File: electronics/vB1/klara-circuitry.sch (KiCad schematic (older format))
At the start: 15 parts, among them J1 Pin header, U1 MCP1700-3302E, U3 ATtiny85

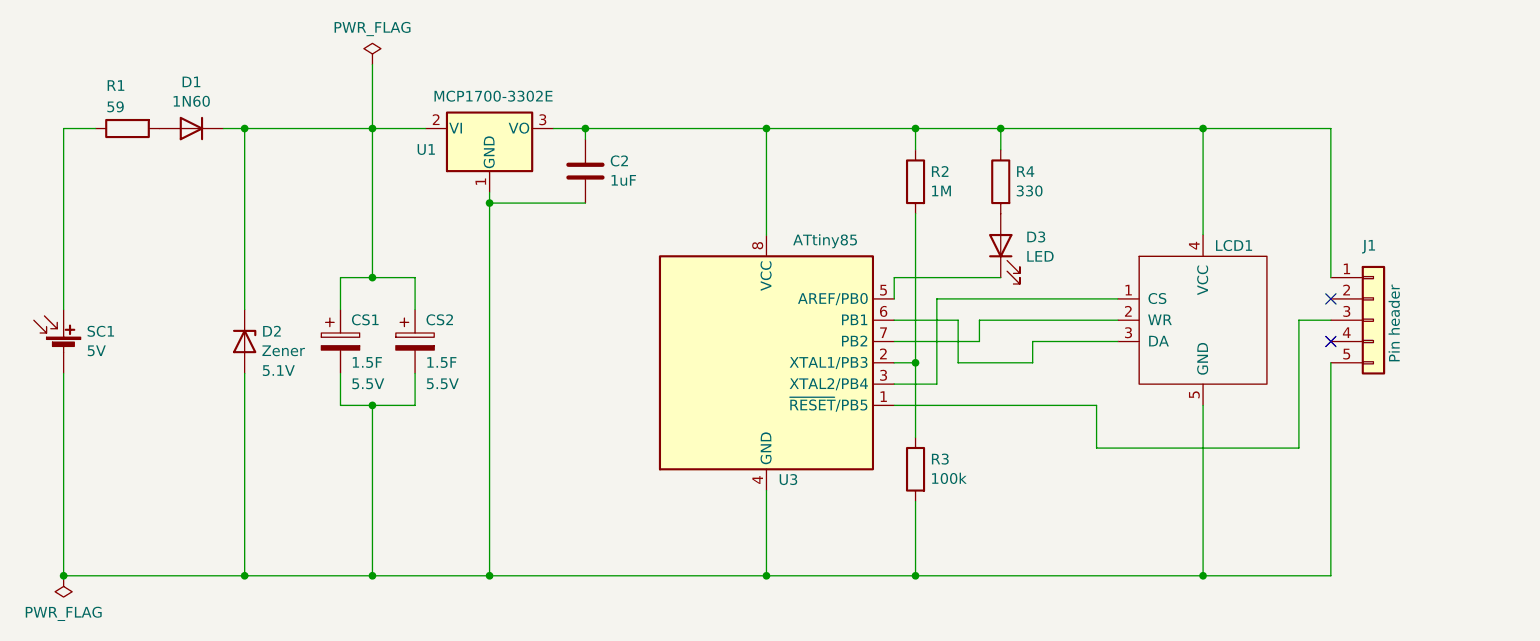
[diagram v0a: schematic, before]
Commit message: circuit d'oh: measure supercap voltage, not regulator output
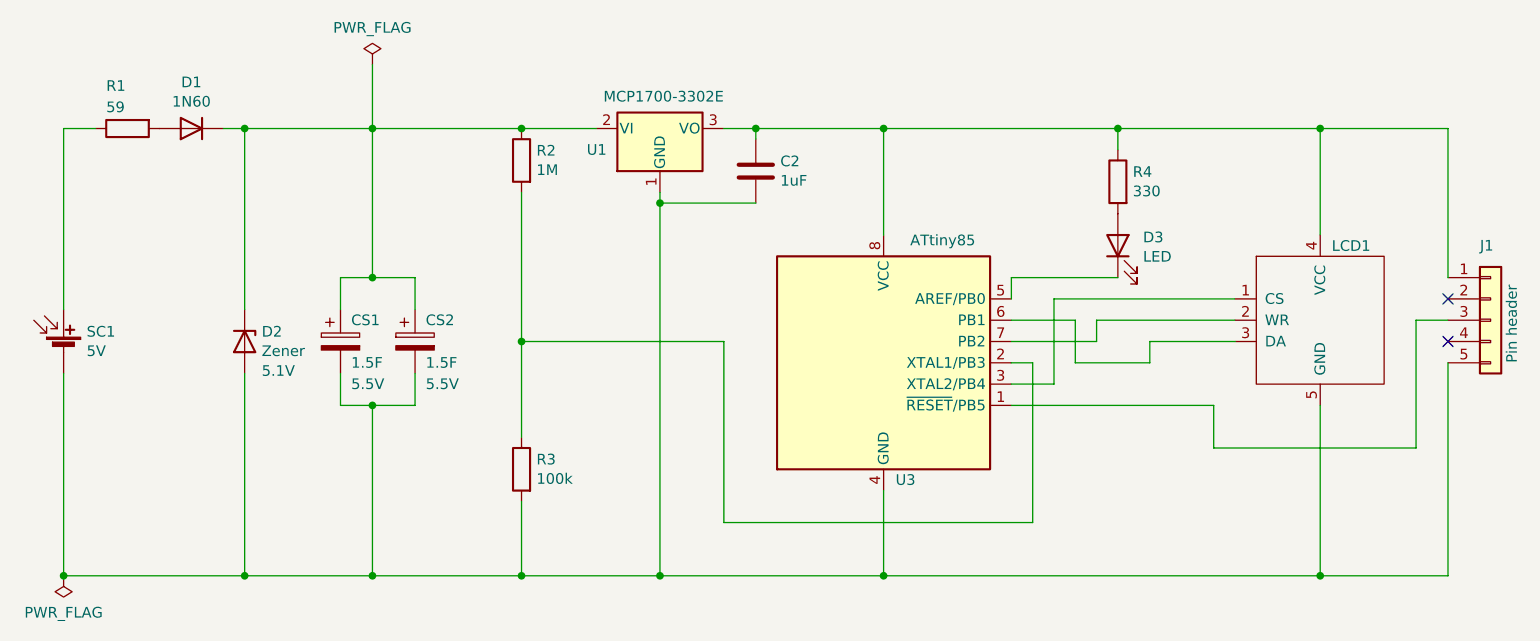
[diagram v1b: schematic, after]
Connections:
- net at C2.1, J1.1 (Pin_1), LCD1.4 (VCC)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: no longer R2.1
- net at CS1.1, CS2.1, D1.1 (K)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: now also R2.1
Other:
- moved on the sheet: C2, D3, J1, LCD1, R2, R3, R4, U1, U3
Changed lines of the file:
@@
 	1500 2600 1500 1750
 Wire Wire Line
-	4800 3450 4800 3850
+	5350 3450 5350 3850
 $Comp
 L Device:D_Zener D2
@@
 $EndComp
 Wire Wire Line
-	4800 1750 4800 2250
-Wire Wire Line
-	5600 2950 5600 2550
+	5350 1750 5350 2250
+Wire Wire Line
+	6150 2950 6150 2550
 $Comp
 L Display_Character:HT1621 LCD1
 U 1 1 62A78604
-P 6850 2750
-F 0 "LCD1" H 6904 3228 50  0000 L TNN
-F 1 "HT1621" H 7178 2805 50  0001 L CNN
-F 2 "Display_7Segment:LCD_SPI" H 7050 3200 50  0001 C CNN
-F 3 "" H 7050 3200 50  0001 C CNN
-	1    6850 2750
-	1    0    0    -1
-$EndComp
-Wire Wire Line
-	5400 2650 5700 2650
-Wire Wire Line
-	5400 2950 5600 2950
+P 7400 2750
+F 0 "LCD1" H 7454 3228 50  0000 L TNN
+F 1 "HT1621" H 7728 2805 50  0001 L CNN
+F 2 "Display_7Segment:LCD_SPI" H 7600 3200 50  0001 C CNN
+F 3 "" H 7600 3200 50  0001 C CNN
+	1    7400 2750
+	1    0    0    -1
+$EndComp
+Wire Wire Line
+	5950 2650 6250 2650
+Wire Wire Line
+	5950 2950 6150 2950
 Wire Wire Line
 	1500 3850 1500 2900
@@
 L Regulator_Linear:MCP1700-3302E_TO92 U1
 U 1 1 62AF9A6C
-P 3500 1750
-F 0 "U1" H 3250 1850 50  0000 R CNN
-F 1 "MCP1700-3302E" H 3800 1600 50  0000 R CNN
-F 2 "Package_TO_SOT_THT:TO-92_Inline_Wide" H 3500 1550 50  0001 C CIN
-F 3 "http://ww1.microchip.com/downloads/en/DeviceDoc/20001826D.pdf" H 3500 1750 50  0001 C CNN
-	1    3500 1750
+P 4300 1750
+F 0 "U1" H 4050 1850 50  0000 R CNN
+F 1 "MCP1700-3302E" H 4600 1600 50  0000 R CNN
+F 2 "Package_TO_SOT_THT:TO-92_Inline_Wide" H 4300 1550 50  0001 C CIN
+F 3 "http://ww1.microchip.com/downloads/en/DeviceDoc/20001826D.pdf" H 4300 1750 50  0001 C CNN
+	1    4300 1750
 	1    0    0    1
 $EndComp
 Wire Wire Line
-	5700 2850 5700 2650
-Wire Wire Line
-	3500 2050 3500 2100
-Wire Wire Line
-	5800 2650 5800 2750
-Wire Wire Line
-	5800 2750 5400 2750
+	6250 2850 6250 2650
+Wire Wire Line
+	4300 2050 4300 2100
+Wire Wire Line
+	6350 2650 6350 2750
+Wire Wire Line
+	6350 2750 5950 2750
 $Comp
 L Device:R R4
 U 1 1 62B13E26
-P 5900 2000
-F 0 "R4" H 5830 2046 50  0000 R CNN
-F 1 "330" H 5830 1955 50  0000 R CNN
-F 2 "Resistor_THT:R_Axial_DIN0207_L6.3mm_D2.5mm_P10.16mm_Horizontal" V 5830 2000 50  0001 C CNN
-F 3 "~" H 5900 2000 50  0001 C CNN
-	1    5900 2000
+P 6450 2000
+F 0 "R4" H 6380 2046 50  0000 R CNN
+F 1 "330" H 6380 1955 50  0000 R CNN
+F 2 "Resistor_THT:R_Axial_DIN0207_L6.3mm_D2.5mm_P10.16mm_Horizontal" V 6380 2000 50  0001 C CNN
+F 3 "~" H 6450 2000 50  0001 C CNN
+	1    6450 2000
 	-1   0    0    -1
 $EndComp
@@
 L Device:LED D3
 U 1 1 62B14898
-P 5900 2300
-F 0 "D3" V 5939 2182 50  0000 R CNN
-F 1 "LED" V 5848 2182 50  0000 R CNN
-F 2 "LED_THT:LED_D5.0mm" H 5900 2300 50  0001 C CNN
-F 3 "~" H 5900 2300 50  0001 C CNN
-	1    5900 2300
+P 6450 2300
+F 0 "D3" V 6489 2182 50  0000 R CNN
+F 1 "LED" V 6398 2182 50  0000 R CNN
+F 2 "LED_THT:LED_D5.0mm" H 6450 2300 50  0001 C CNN
+F 3 "~" H 6450 2300 50  0001 C CNN
+	1    6450 2300
 	0    -1   -1   0
 $EndComp
 Wire Wire Line
-	4800 1750 5500 1750
-Wire Wire Line
-	3800 1750 3950 1750
+	4600 1750 4750 1750
 $Comp
 L Device:C C2
 U 1 1 62B08E4B
-P 3950 1950
-F 0 "C2" H 4065 1996 50  0000 L CNN
-F 1 "1uF" H 4065 1905 50  0000 L CNN
-F 2 "Capacitor_THT:C_Rect_L7.0mm_W2.0mm_P5.00mm" H 3988 1800 50  0001 C CNN
-F 3 "~" H 3950 1950 50  0001 C CNN
-	1    3950 1950
-	1    0    0    -1
-$EndComp
-Wire Wire Line
-	3950 1800 3950 1750
-Wire Wire Line
-	3950 2100 3500 2100
-Connection ~ 3500 2100
-Wire Wire Line
-	3500 2100 3500 3850
+P 4750 1950
+F 0 "C2" H 4865 1996 50  0000 L CNN
+F 1 "1uF" H 4865 1905 50  0000 L CNN
+F 2 "Capacitor_THT:C_Rect_L7.0mm_W2.0mm_P5.00mm" H 4788 1800 50  0001 C CNN
+F 3 "~" H 4750 1950 50  0001 C CNN
+	1    4750 1950
+	1    0    0    -1
+$EndComp
+Wire Wire Line
+	4750 1800 4750 1750
+Wire Wire Line
+	4750 2100 4300 2100
+Connection ~ 4300 2100
+Wire Wire Line
+	4300 2100 4300 3850
 $Comp
 L Device:R R2
 U 1 1 62B0AC42
-P 5500 2000
-F 0 "R2" H 5430 2046 50  0000 R CNN
-F 1 "1M" H 5430 1955 50  0000 R CNN
-F 2 "Resistor_THT:R_Axial_DIN0207_L6.3mm_D2.5mm_P10.16mm_Horizontal" V 5430 2000 50  0001 C CNN
-F 3 "~" H 5500 2000 50  0001 C CNN
-	1    5500 2000
+P 3650 1900
+F 0 "R2" H 3580 1946 50  0000 R CNN
+F 1 "1M" H 3580 1855 50  0000 R CNN
+F 2 "Resistor_THT:R_Axial_DIN0207_L6.3mm_D2.5mm_P10.16mm_Horizontal" V 3580 1900 50  0001 C CNN
+F 3 "~" H 3650 1900 50  0001 C CNN
+	1    3650 1900
 	-1   0    0    -1
 $EndComp
@@
 L Device:R R3
 U 1 1 62B0C047
-P 5500 3350
-F 0 "R3" H 5430 3396 50  0000 R CNN
-F 1 "100k" H 5430 3305 50  0000 R CNN
-F 2 "Resistor_THT:R_Axial_DIN0207_L6.3mm_D2.5mm_P10.16mm_Horizontal" V 5430 3350 50  0001 C CNN
-F 3 "~" H 5500 3350 50  0001 C CNN
-	1    5500 3350
+P 3650 3350
+F 0 "R3" H 3580 3396 50  0000 R CNN
+F 1 "100k" H 3580 3305 50  0000 R CNN
+F 2 "Resistor_THT:R_Axial_DIN0207_L6.3mm_D2.5mm_P10.16mm_Horizontal" V 3580 3350 50  0001 C CNN
+F 3 "~" H 3650 3350 50  0001 C CNN
+	1    3650 3350
 	-1   0    0    -1
 $EndComp
 Wire Wire Line
-	5500 1850 5500 1750
-Connection ~ 5500 1750
-Wire Wire Line
-	5400 2850 5500 2850
-Wire Wire Line
-	5500 2850 5500 2150
+	5950 2850 6050 2850
 Connection ~ 2350 3850
 Wire Wire Line
@@
 Connection ~ 2350 1750
 Wire Wire Line
-	5500 1750 5900 1750
-Wire Wire Line
-	5900 1850 5900 1750
-Wire Wire Line
-	5900 2450 5400 2450
-Wire Wire Line
-	5400 2450 5400 2550
-Wire Wire Line
-	5700 2850 6050 2850
-Wire Wire Line
-	6050 2850 6050 2750
-Wire Wire Line
-	5600 2550 6450 2550
-Wire Wire Line
-	5800 2650 6450 2650
-Wire Wire Line
-	6050 2750 6450 2750
-Wire Wire Line
-	5400 3050 6350 3050
-Wire Wire Line
-	6850 3850 6850 3050
-Connection ~ 5900 1750
-Wire Wire Line
-	6850 1750 6850 2250
+	6450 1850 6450 1750
+Wire Wire Line
+	6450 2450 5950 2450
+Wire Wire Line
+	5950 2450 5950 2550
+Wire Wire Line
+	6250 2850 6600 2850
+Wire Wire Line
+	6600 2850 6600 2750
+Wire Wire Line
+	6150 2550 7000 2550
+Wire Wire Line
+	6350 2650 7000 2650
+Wire Wire Line
+	6600 2750 7000 2750
+Wire Wire Line
+	5950 3050 6900 3050
+Wire Wire Line
+	7400 3850 7400 3050
+Connection ~ 6450 1750
+Wire Wire Line
+	7400 1750 7400 2250
 Wire Wire Line
 	2350 3850 2950 3850
@@
 Connection ~ 2950 3850
 Wire Wire Line
-	2950 3850 3500 3850
-Wire Wire Line
 	2950 2450 2950 1750
 Wire Wire Line
@@
 Connection ~ 2950 1750
 Wire Wire Line
-	2950 1750 3200 1750
-Wire Wire Line
-	6850 3850 7450 3850
-Connection ~ 6850 3850
-Wire Wire Line
-	7300 2650 7300 3250
-Wire Wire Line
-	7300 3250 6350 3250
-Wire Wire Line
-	6350 3250 6350 3050
-Wire Wire Line
-	7300 2650 7450 2650
-Wire Wire Line
-	6850 1750 7450 1750
-Connection ~ 6850 1750
-Wire Wire Line
-	4800 3850 5500 3850
-Wire Wire Line
-	5500 2850 5500 3200
-Connection ~ 5500 2850
-Wire Wire Line
-	5500 3500 5500 3850
-Connection ~ 5500 3850
-Wire Wire Line
-	5500 3850 6850 3850
+	7400 3850 8000 3850
+Connection ~ 7400 3850
+Wire Wire Line
+	7850 2650 7850 3250
+Wire Wire Line
+	7850 3250 6900 3250
+Wire Wire Line
+	6900 3250 6900 3050
+Wire Wire Line
+	7850 2650 8000 2650
+Wire Wire Line
+	7400 1750 8000 1750
+Connection ~ 7400 1750
+Wire Wire Line
+	3650 3500 3650 3850
 $Comp
 L MCU_Microchip_ATtiny:ATtiny85-20PU U3
 U 1 1 62A64AD0
-P 4800 2850
-F 0 "U3" H 4950 2300 50  0000 R CNN
-F 1 "ATtiny85" H 5231 3425 50  0000 R CNN
-F 2 "Package_DIP:DIP-8_W7.62mm" H 4800 2850 50  0001 C CIN
-F 3 "http://ww1.microchip.com/downloads/en/DeviceDoc/atmel-2586-avr-8-bit-microcontroller-attiny25-attiny45-attiny85_datasheet.pdf" H 4800 2850 50  0001 C CNN
-	1    4800 2850
+P 5350 2850
+F 0 "U3" H 5500 2300 50  0000 R CNN
+F 1 "ATtiny85" H 5781 3425 50  0000 R CNN
+F 2 "Package_DIP:DIP-8_W7.62mm" H 5350 2850 50  0001 C CIN
+F 3 "http://ww1.microchip.com/downloads/en/DeviceDoc/atmel-2586-avr-8-bit-microcontroller-attiny25-attiny45-attiny85_datasheet.pdf" H 5350 2850 50  0001 C CNN
+	1    5350 2850
 	1    0    0    -1
 $EndComp
@@
 	2950 1450 2950 1750
 Wire Wire Line
-	5900 1750 6850 1750
-Wire Wire Line
-	3950 1750 4800 1750
-Connection ~ 3950 1750
-Connection ~ 4800 1750
-Wire Wire Line
-	3500 3850 4800 3850
-Connection ~ 3500 3850
-Connection ~ 4800 3850
+	6450 1750 7400 1750
 $Comp
 L Connector_Generic:Conn_01x05 J1
 U 1 1 62D16CCC
-P 7650 2650
-F 0 "J1" H 7600 3000 50  0000 L CNN
-F 1 "Pin header" V 7750 2450 50  0000 L CNN
-F 2 "Connector_PinHeader_2.54mm:PinHeader_1x05_P2.54mm_Vertical" H 7650 2650 50  0001 C CNN
-F 3 "~" H 7650 2650 50  0001 C CNN
-	1    7650 2650
-	1    0    0    -1
-$EndComp
-Wire Wire Line
-	7450 2850 7450 3850
-Wire Wire Line
-	7450 1750 7450 2450
-NoConn ~ 7450 2550
-NoConn ~ 7450 2750
+P 8200 2650
+F 0 "J1" H 8150 3000 50  0000 L CNN
+F 1 "Pin header" V 8300 2450 50  0000 L CNN
+F 2 "Connector_PinHeader_2.54mm:PinHeader_1x05_P2.54mm_Vertical" H 8200 2650 50  0001 C CNN
+F 3 "~" H 8200 2650 50  0001 C CNN
+	1    8200 2650
+	1    0    0    -1
+$EndComp
+Wire Wire Line
+	8000 2850 8000 3850
+Wire Wire Line
+	8000 1750 8000 2450
+NoConn ~ 8000 2550
+NoConn ~ 8000 2750
+Wire Wire Line
+	5350 3850 7400 3850
+Wire Wire Line
+	2950 3850 3650 3850
+Connection ~ 5350 3850
+Connection ~ 3650 3850
+Wire Wire Line
+	3650 3850 4300 3850
+Connection ~ 4300 3850
+Wire Wire Line
+	4300 3850 5350 3850
+Wire Wire Line
+	2950 1750 3650 1750
+Connection ~ 3650 1750
+Wire Wire Line
+	3650 1750 4000 1750
+Wire Wire Line
+	4750 1750 5350 1750
+Connection ~ 4750 1750
+Connection ~ 5350 1750
+Wire Wire Line
+	3650 2050 3650 2750
+Wire Wire Line
+	3650 2750 4600 2750
+Wire Wire Line
+	4600 2750 4600 3600
+Wire Wire Line
+	4600 3600 6050 3600
+Wire Wire Line
+	6050 2850 6050 3600
+Connection ~ 3650 2750
+Wire Wire Line
+	3650 2750 3650 3200
+Wire Wire Line
+	5350 1750 6450 1750
 $EndSCHEMATC
